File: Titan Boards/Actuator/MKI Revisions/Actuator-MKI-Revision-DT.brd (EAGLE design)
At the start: 101.6 x 101.6 mm, 108 parts, among them U1 DRV8816PWPR, U2 W25Q128BVEIG, Y2 16MHz

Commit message: Update Actuator-MKI-Revision-DT.brd
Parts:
- moved C2 6.10 mm to (39.1, 65.3)
- moved R7 3.79 mm to (60.2, 59.8)
- moved R6 3.70 mm to (57.5, 59.8)
- moved C3 2.79 mm to (39.1, 63.2)
- moved R44 2.09 mm to (37.2, 56.4)
- moved R12 1.72 mm to (37.6, 54.1)
- moved R5 1.62 mm to (43.6, 63.9)
- turned Y2 to 0 degrees
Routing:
- net N$2: track 7.08 -> 0.00 mm
- net N$29: track 6.73 -> 0.53 mm
- net USB_DN: track 49.1 -> 53.1 mm
- net USB_DP: track 48.7 -> 52.4 mm
- net N$3: track 3.35 -> 0.00 mm
- net N$12: track 3.17 -> 0.27 mm
- net +3V3: track 226.6 -> 229.2 mm
- net AGND: track 79.7 -> 81.8 mm
- net PWM_CLAW: track 58.2 -> 60.0 mm
- net N$33: track 15.8 -> 14.1 mm
- net N$35: track 10.6 -> 8.92 mm
- net N$36: track 16.5 -> 18.2 mm
- net N$34: track 13.8 -> 15.2 mm
- net PWM_DRIVER2: track 18.1 -> 16.7 mm
- net QSPI_SD3: track 22.0 -> 23.3 mm
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- added copper zone on layer 1, net N$52

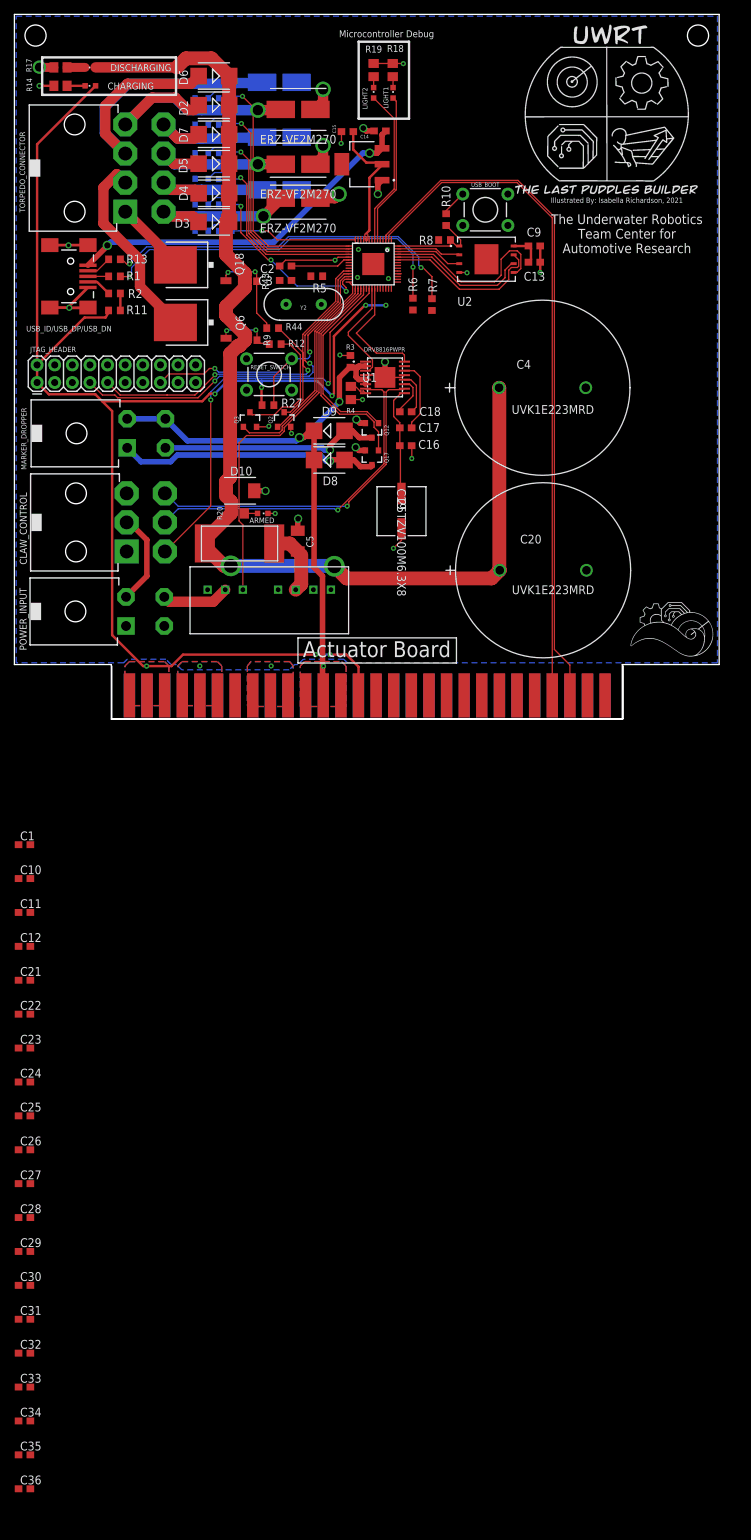
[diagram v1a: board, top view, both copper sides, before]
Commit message: Adjusted wires for design rules
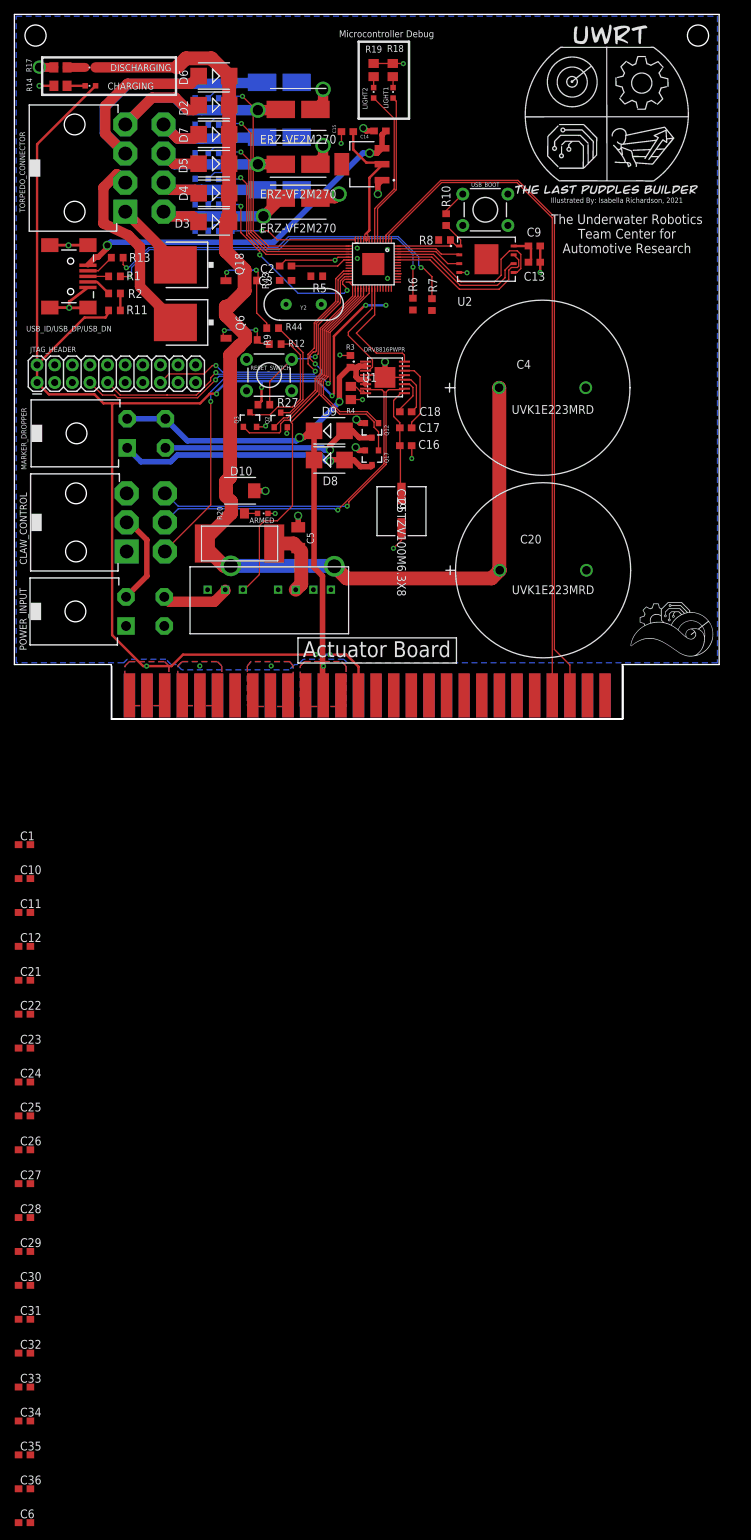
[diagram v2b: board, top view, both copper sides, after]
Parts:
- added C6: 10uF, rcl:C0603
- C1, C11, C21, C23, C25, C27, C32, C34: value 10 uF -> .1 uF
- C36: value 0.1uF -> 10uF
- moved R27 0.60 mm to (36.0, 45.3)
- moved C5 0.50 mm to (40.9, 26.2)
- moved Q2 0.50 mm to (38.4, 43.1)
- moved R13 0.46 mm to (14.8, 66.5)
- moved R43 0.10 mm to (34.1, 63.2)
- moved RESET_SWITCH 0.10 mm to (36.7, 49.6)
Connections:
- net +3V3: no longer USB_BOOT.3
- net AGND: now also C6.1, USB_BOOT.3
- net QSPI_SS: now also C6.2
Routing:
- net +24V: track 167.1 -> 169.2 mm
- net ARM_TORPEDO: track 53.6 -> 51.7 mm
- net SWD_CLK: track 49.2 -> 50.5 mm
- net SWD_IO: track 52.5 -> 53.8 mm
- net TORPEDO2: track 28.2 -> 29.0 mm
- net N$33: track 14.1 -> 14.8 mm
- net USB_DN: track 53.1 -> 53.8 mm
- net RESET: track 45.7 -> 46.4 mm
- net COIL_4_GATE: track 30.8 -> 31.4 mm
- net N$34: track 15.2 -> 15.7 mm
- net TORPEDO1_GATE: track 25.7 -> 26.2 mm
- net N$35: track 8.92 -> 9.42 mm

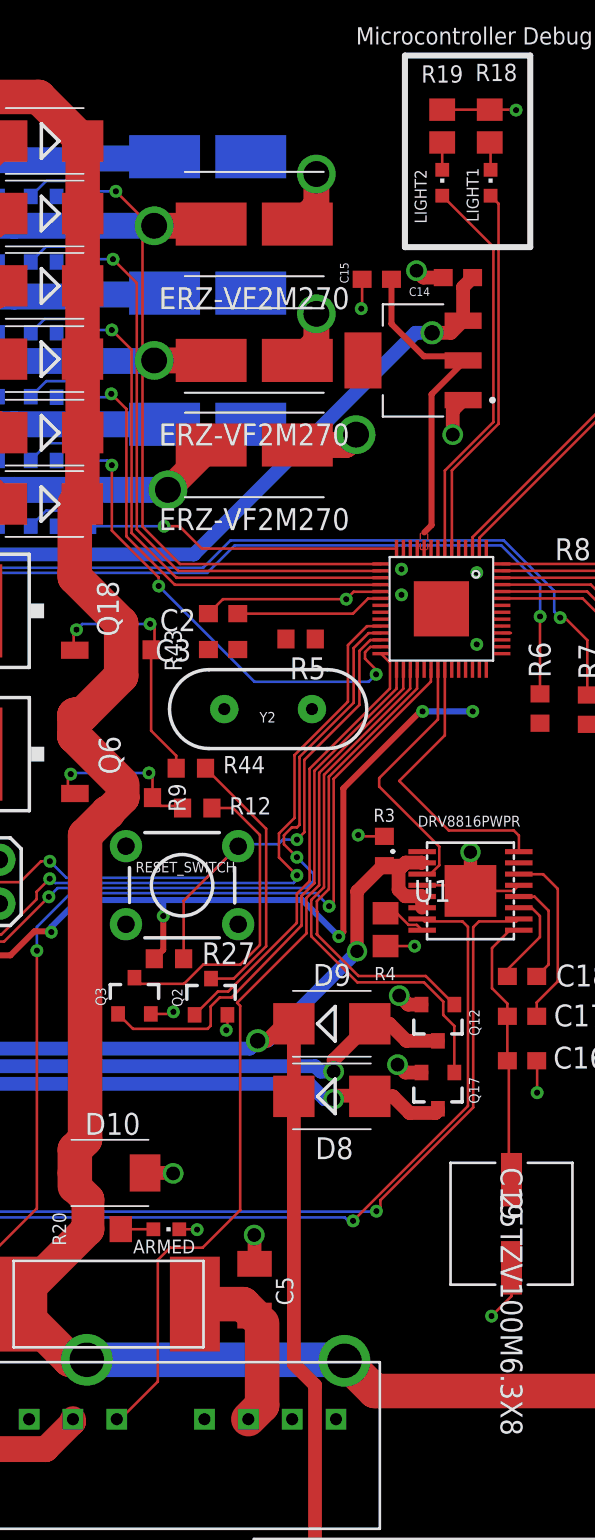
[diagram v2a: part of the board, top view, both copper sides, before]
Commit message: Updated wire routings to meet design rule requirements
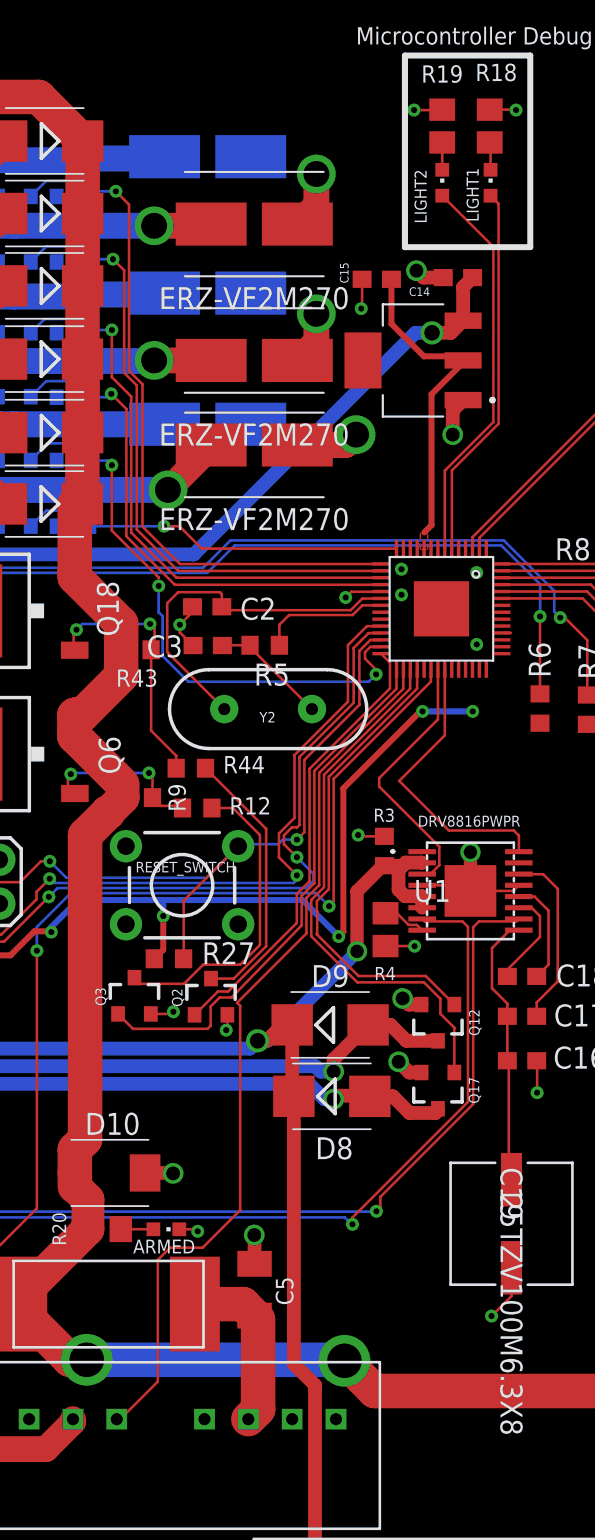
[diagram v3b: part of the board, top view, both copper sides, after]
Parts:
- moved R5 2.11 mm to (41.5, 63.5)
- moved C2 1.01 mm to (38.2, 65.7)
- moved C3 0.92 mm to (38.2, 63.5)
- moved D9 0.12 mm to (45.3, 41.5)
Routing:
- net N$11: track 8.66 -> 21.3 mm
- net N$3: track 0.00 -> 7.54 mm
- net N$2: track 0.00 -> 6.79 mm
- net AGND: track 81.4 -> 75.1 mm, vias 28 -> 30
- net COIL_4_GATE: track 31.4 -> 33.7 mm

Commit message: Actuator work
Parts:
- moved C6 196.9 mm to (60.3, 72.1), turned to 270 degrees
- moved C36 179.2 mm to (44.5, 63.0), turned to 270 degrees
- moved C33 175.7 mm to (56.4, 70.6), flipped to the bottom, turned to 90 degrees
- moved C35 174.4 mm to (51.5, 61.0), flipped to the bottom, turned to 270 degrees
- moved C32 170.4 mm to (54.2, 70.6), flipped to the bottom, turned to 90 degrees
- moved C34 170.4 mm to (53.8, 61.0), flipped to the bottom, turned to 270 degrees
- moved C31 150.9 mm to (49.1, 56.7), flipped to the bottom, turned to 90 degrees
- moved C28 150.5 mm to (49.9, 70.6), flipped to the bottom, turned to 90 degrees
- moved C27 146.6 mm to (52.1, 70.6), flipped to the bottom, turned to 90 degrees
- moved C30 146.3 mm to (51.9, 55.7), flipped to the bottom, turned to 180 degrees
- moved C29 143.7 mm to (51.9, 57.9), flipped to the bottom, turned to 180 degrees
- moved C26 133.0 mm to (47.1, 62.9), flipped to the bottom
- moved C25 130.5 mm to (47.1, 65.0), flipped to the bottom
- moved C24 128.2 mm to (56.6, 63.4), flipped to the bottom, turned to 180 degrees
- moved C23 121.8 mm to (56.6, 61.2), flipped to the bottom, turned to 180 degrees
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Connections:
- removed net N$24: C11.1, C12.1, U$9.P$22
- removed net N$30: C21.1, C22.1, U$9.P$48, U$9.P$49
- removed net N$5: C1.1, C10.1, U$9.P$33
- removed net N$50: C23.1, C24.1, U$9.P$43, U$9.P$44
- removed net N$51: C27.1, C28.1, U$9.P$1
- removed net N$52: C25.1, C26.1, U$9.P$10
- removed net N$53: C32.1, C33.1, U$9.P$45, U$9.P$50
- removed net N$54: C34.1, C35.1, U$9.P$23
- removed net N$55: C29.1, C30.1, C31.2, U$9.P$42
- net +3V3: now also C1.1, C10.1, C11.1, C12.1, C21.1, C22.1, C23.1, C24.1, C25.1, C26.1, C27.1, C28.1, C29.1, C30.1, C31.2, C32.1, C33.1, C34.1, C35.1, U$9.P$1, U$9.P$10, U$9.P$22, U$9.P$23, U$9.P$33, U$9.P$42, U$9.P$43, U$9.P$44, U$9.P$45, U$9.P$48, U$9.P$49, U$9.P$50
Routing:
- net +3V3: track 228.8 -> 293.2 mm, vias 8 -> 16
- net +5V: track 86.9 -> 81.0 mm
- net USB_DN: track 53.8 -> 58.2 mm
- net USB_DP: track 52.4 -> 56.0 mm
- net AGND: track 75.1 -> 77.9 mm, vias 30 -> 31
- net QSPI_SS: track 14.0 -> 16.1 mm
- net N$29: track 0.53 -> 2.31 mm
- net RESET: track 46.4 -> 48.1 mm, vias 2 -> 3
- net N$12: track 0.27 -> 1.48 mm
- net QSPI_SD3: track 23.3 -> 22.4 mm
- net QSPI_SCLK: track 20.4 -> 19.6 mm
- net QSPI_SD0: track 26.1 -> 25.5 mm
- removed copper zone on layer 1, net N$52

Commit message: Actuator board review final revisions
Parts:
- moved R4 0.79 mm to (48.5, 46.2)
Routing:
- net +3V3: track 293.2 -> 325.0 mm
- net RESET: track 48.1 -> 50.8 mm, vias 3 -> 4
- net PWM_DRIVER2: track 16.7 -> 14.6 mm
- net +24V: track 169.2 -> 167.2 mm
- net AGND: track 77.9 -> 79.5 mm, vias 31 -> 32
- net COIL_1: track 23.2 -> 24.2 mm
- net COIL_2: track 21.3 -> 22.2 mm
- net TORPEDO2: track 29.0 -> 28.2 mm
- net COIL_S: track 38.0 -> 38.7 mm
- net COIL_3: track 24.0 -> 24.6 mm
- net COIL_5_GATE: track 40.6 -> 41.1 mm
- net PWM_DRIVER1: track 15.6 -> 16.0 mm, vias 0 -> 2

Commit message: Actuator MKI revision order version
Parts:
- moved C15 10.5 mm to (50.3, 74.5)
- moved R13 0.77 mm to (14.4, 65.9)
- moved R3 0.66 mm to (47.8, 51.6)
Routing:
- net AGND: track 79.5 -> 76.8 mm, vias 32 -> 35
- net +3V3: track 325.0 -> 326.6 mm, vias 16 -> 17
- net PWM_DRIVER1: track 16.0 -> 14.8 mm
